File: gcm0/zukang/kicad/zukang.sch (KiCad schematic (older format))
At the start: 109 parts, among them J1 RX, J2 TX, Q1 BC547, Q2 BC547, Q3 BC547, SW1 SW_Push, SW2 SW_Push, U1 74HC595, U10 F5161BS, U11 TL084, U12 TL084, U13 L7805, U14 L7905, U15 LM1117-3.3, U16 STM32F030F4P6, U17 STM32F030F4P6, U2 74HC595, U3 ne602, U4 F5161BS, U5 ne602, U6 CD4052B, U7 F5161BS, U8 F5161BS, U9 F5161BS, Y1 8M, Y2 8M

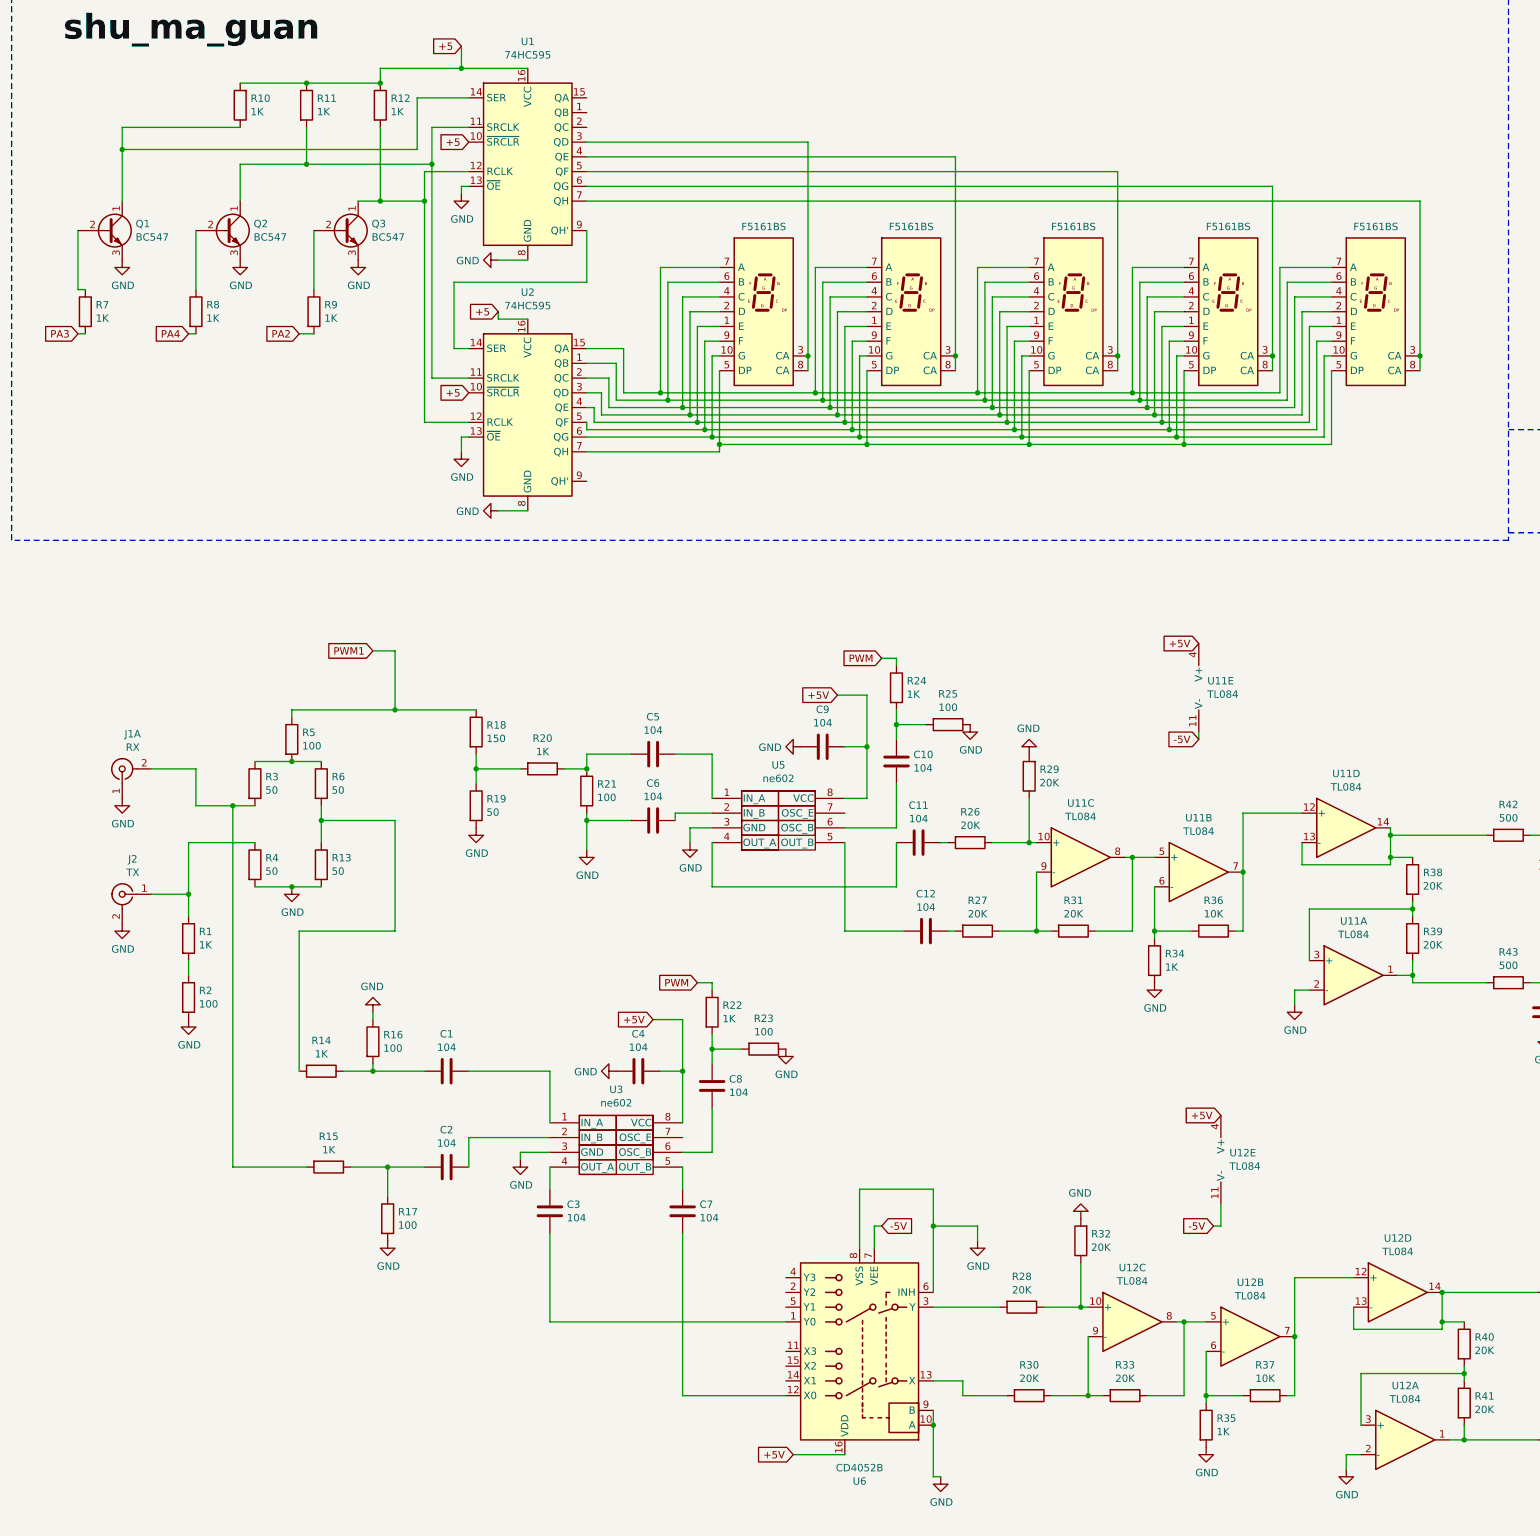
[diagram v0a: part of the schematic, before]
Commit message: 电路改错
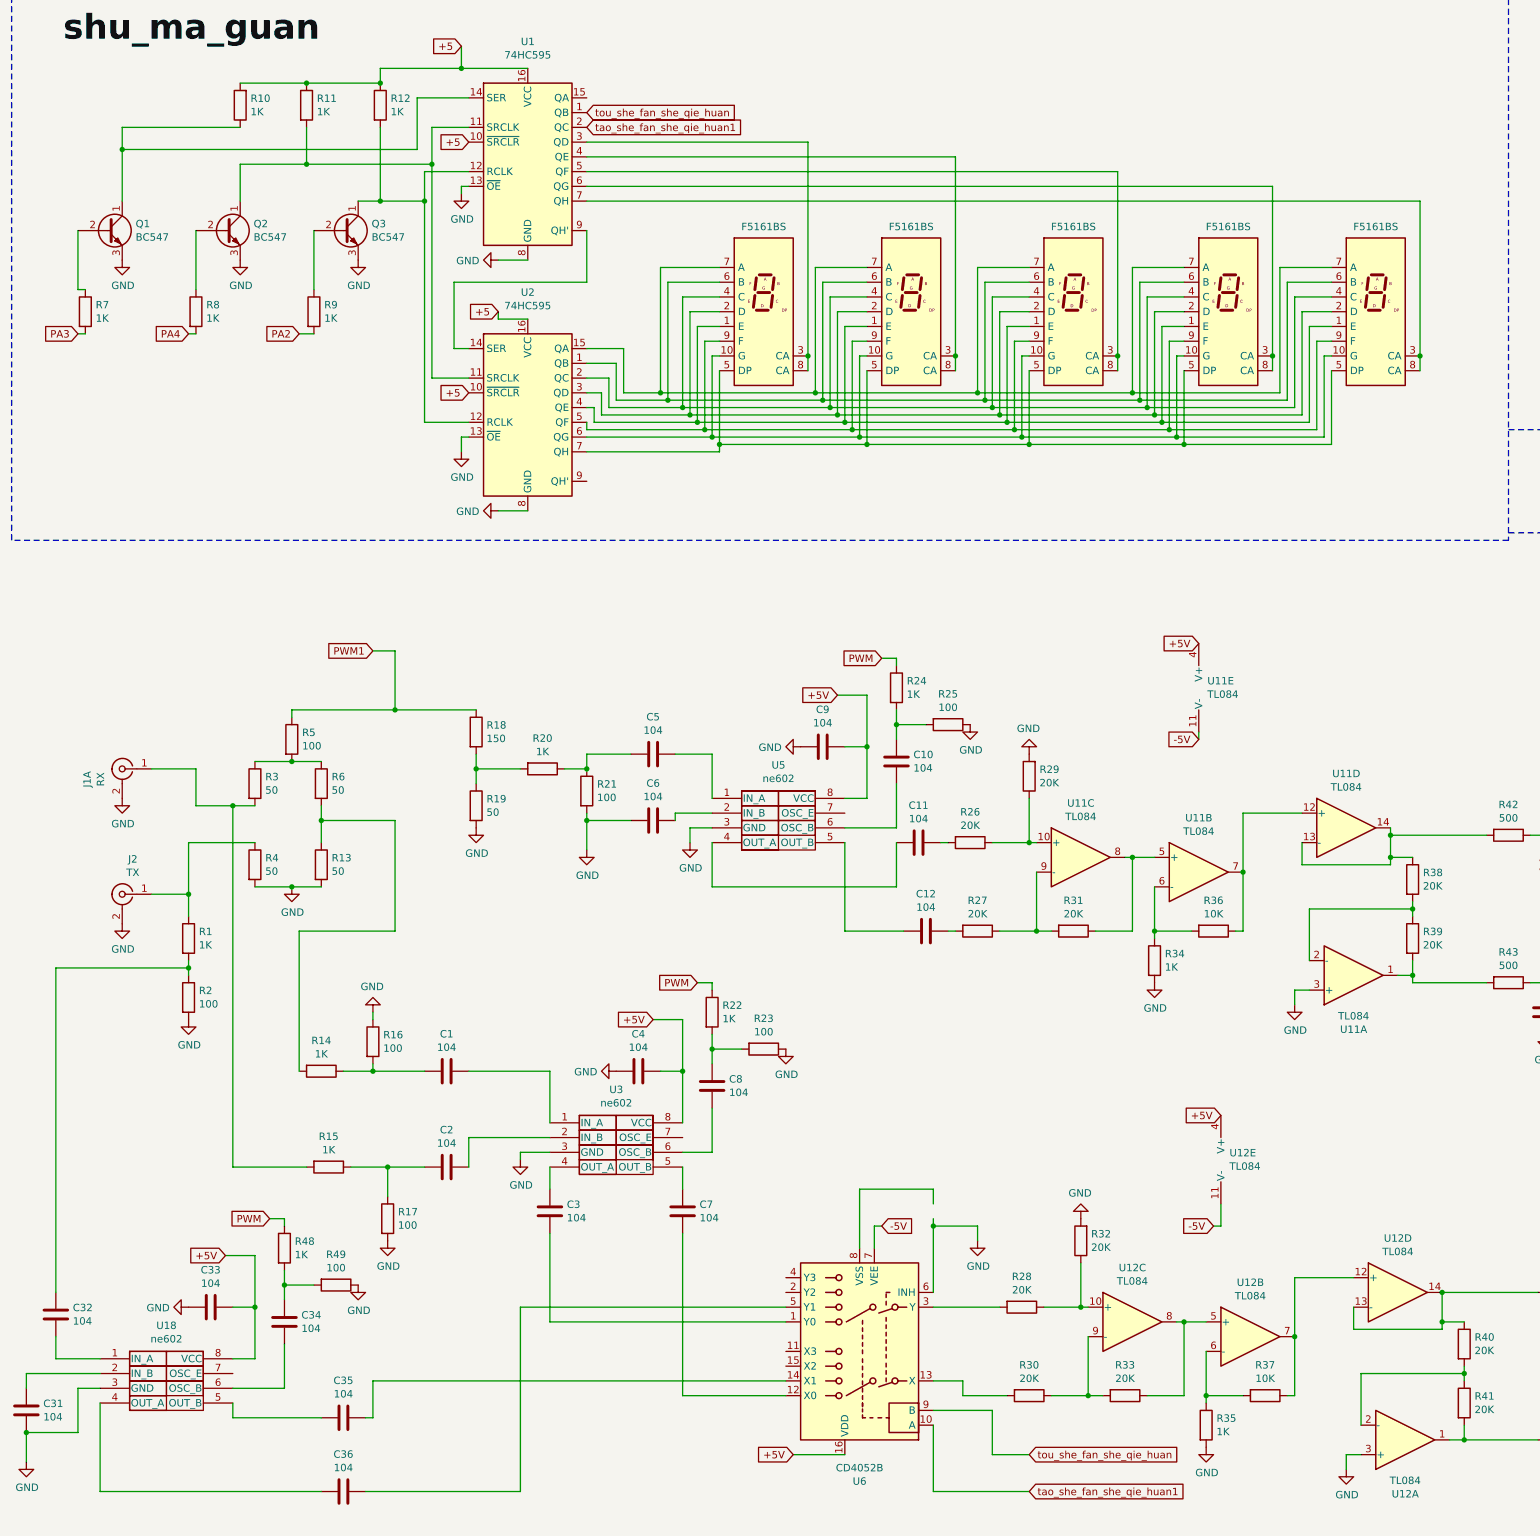
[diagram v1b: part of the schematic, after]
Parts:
- added C31, C32, C33, C34, C35, C36: 104, symbol Device:C
- added R48: 1K, symbol Device:R
- added R49: 100, symbol Device:R
- added U18: ne602, symbol 1-cache:yjmwxwx_ne602
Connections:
- net +5V: now also C33.2, U18.8 (VCC)
- net GND: now also J1.2 (Ext1), U11.3 (+), U12.3 (+), C31.2, C33.1, R49.1, U18.3 (GND); no longer J1.1 (In1), U11.2 (-), U12.2 (-), U6.10 (A), U6.8 (VSS), U6.9 (B)
- net PWM: now also R48.1
- net tou_she_fan_she_qie_huan: now reaches U1.1 (QB)
- net tou_she_fan_she_qie_huan: now also U6.9 (B)
- net tao_she_fan_she_qie_huan1: now reaches U1.2 (QC)
- net tao_she_fan_she_qie_huan1: now also U6.10 (A)
- net at U6.14 (X1): now also C35.1
- net at U6.5 (Y1): now also C36.1
- net at R38.2, R39.1: now also U11.2 (-); no longer U11.3 (+)
- net at R40.2, R41.1: now also U12.2 (-); no longer U12.3 (+)
- net at R15.2, R3.2: now also J1.1 (In1); no longer J1.2 (Ext1)
- net at R1.2, R2.1: now also C32.1
- new net: C32.2, U18.1 (IN_A)
- new net: C31.1, U18.2 (IN_B)
- new net: C36.2, U18.4 (OUT_A)
- new net: C35.2, U18.5 (OUT_B)
- new net: C34.2, U18.6 (OSC_B)
- new net: C34.1, R48.2, R49.2
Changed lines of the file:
@@
 F 3 "http://www.ti.com/lit/ds/symlink/tl081.pdf" H 9700 7450 50  0001 C CNN
 	1    9650 7250
-	1    0    0    -1
+	1    0    0    1
 $EndComp
 $Comp
@@
 F 3 "http://www.ti.com/lit/ds/symlink/tl081.pdf" H 10050 10600 50  0001 C CNN
 	1    10000 10400
-	1    0    0    -1
+	1    0    0    1
 $EndComp
 $Comp
@@
 	6300 8700 6800 8700
 Wire Wire Line
-	6800 8700 6800 8950
+	6800 8700 6800 8800
 $Comp
 L power:GND #PWR0127
@@
 Wire Wire Line
 	6400 8950 6450 8950
-$Comp
-L power:GND #PWR0128
-U 1 1 5FA99091
-P 6850 10650
-F 0 "#PWR0128" H 6850 10400 50  0001 C CNN
-F 1 "GND" H 6855 10477 50  0000 C CNN
-F 2 "" H 6850 10650 50  0001 C CNN
-F 3 "" H 6850 10650 50  0001 C CNN
-	1    6850 10650
-	1    0    0    -1
-$EndComp
-Wire Wire Line
-	6800 10200 6800 10300
-Wire Wire Line
-	6800 10300 6800 10650
-Wire Wire Line
-	6800 10650 6850 10650
-Connection ~ 6800 10300
 Text GLabel 5850 10500 0    50   Input ~ 0
 +5V
@@
 F 3 " ~" H 1300 5850 50  0001 C CNN
 	1    1300 5850
-	0    -1   -1   0
+	-1   0    0    -1
 $EndComp
 $Comp
@@
 $EndComp
 Wire Wire Line
-	1750 7250 1750 7150
+	1750 7250 1750 7200
 Wire Wire Line
 	1750 6850 1750 6700
@@
 Wire Notes Line
 	16000 500  16000 9900
+$Comp
+L 1-cache:yjmwxwx_ne602 U18
+U 1 1 5E485B54
+P 1600 10000
+F 0 "U18" H 1600 10375 50  0000 C CNN
+F 1 "ne602" H 1600 10284 50  0000 C CNN
+F 2 "" H 1550 10300 50  0001 C CNN
+F 3 "" H 1550 10300 50  0001 C CNN
+	1    1600 10000
+	1    0    0    -1
+$EndComp
+$Comp
+L Device:C C36
+U 1 1 5E485B68
+P 2800 10750
+F 0 "C36" V 2548 10750 50  0000 C CNN
+F 1 "104" V 2639 10750 50  0000 C CNN
+F 2 "" H 2838 10600 50  0001 C CNN
+F 3 "~" H 2800 10750 50  0001 C CNN
+	1    2800 10750
+	0    1    1    0
+$EndComp
+$Comp
+L Device:C C35
+U 1 1 5E485B6E
+P 2800 10250
+F 0 "C35" V 2548 10250 50  0000 C CNN
+F 1 "104" V 2639 10250 50  0000 C CNN
+F 2 "" H 2838 10100 50  0001 C CNN
+F 3 "~" H 2800 10250 50  0001 C CNN
+	1    2800 10250
+	0    1    1    0
+$EndComp
+Wire Wire Line
+	2950 10250 3000 10250
+$Comp
+L Device:C C34
+U 1 1 5E485B7B
+P 2400 9600
+F 0 "C34" H 2515 9646 50  0000 L CNN
+F 1 "104" H 2515 9555 50  0000 L CNN
+F 2 "" H 2438 9450 50  0001 C CNN
+F 3 "~" H 2400 9600 50  0001 C CNN
+	1    2400 9600
+	1    0    0    -1
+$EndComp
+Wire Wire Line
+	2400 9750 2400 10050
+Wire Wire Line
+	2400 10050 2050 10050
+$Comp
+L Device:R R48
+U 1 1 5E485B83
+P 2400 9100
+F 0 "R48" H 2470 9146 50  0000 L CNN
+F 1 "1K" H 2470 9055 50  0000 L CNN
+F 2 "" V 2330 9100 50  0001 C CNN
+F 3 "~" H 2400 9100 50  0001 C CNN
+	1    2400 9100
+	1    0    0    -1
+$EndComp
+$Comp
+L Device:R R49
+U 1 1 5E485B89
+P 2750 9350
+F 0 "R49" V 2543 9350 50  0000 C CNN
+F 1 "100" V 2634 9350 50  0000 C CNN
+F 2 "" V 2680 9350 50  0001 C CNN
+F 3 "~" H 2750 9350 50  0001 C CNN
+	1    2750 9350
+	0    1    1    0
+$EndComp
+Wire Wire Line
+	2400 9250 2400 9350
+Wire Wire Line
+	2600 9350 2400 9350
+Connection ~ 2400 9350
+Wire Wire Line
+	2400 9350 2400 9450
+Text GLabel 2300 8900 0    50   Input ~ 0
+PWM
+Wire Wire Line
+	2300 8900 2400 8900
+Wire Wire Line
+	2400 8900 2400 8950
+Text GLabel 2000 9150 0    50   Input ~ 0
++5V
+$Comp
+L Device:C C33
+U 1 1 5E485B97
+P 1900 9500
+F 0 "C33" V 2152 9500 50  0000 C CNN
+F 1 "104" V 2061 9500 50  0000 C CNN
+F 2 "" H 1938 9350 50  0001 C CNN
+F 3 "~" H 1900 9500 50  0001 C CNN
+	1    1900 9500
+	0    -1   -1   0
+$EndComp
+$Comp
+L power:GND #PWR0144
+U 1 1 5E485B9D
+P 1750 9500
+F 0 "#PWR0144" H 1750 9250 50  0001 C CNN
+F 1 "GND" V 1755 9372 50  0000 R CNN
+F 2 "" H 1750 9500 50  0001 C CNN
+F 3 "" H 1750 9500 50  0001 C CNN
+	1    1750 9500
+	0    1    1    0
+$EndComp
+Wire Wire Line
+	2000 9150 2200 9150
+Wire Wire Line
+	2200 9150 2200 9500
+Wire Wire Line
+	2200 9850 2050 9850
+Wire Wire Line
+	2050 9500 2200 9500
+Connection ~ 2200 9500
+Wire Wire Line
+	2200 9500 2200 9850
+$Comp
+L power:GND #PWR0145
+U 1 1 5E485BB9
+P 650 10550
+F 0 "#PWR0145" H 650 10300 50  0001 C CNN
+F 1 "GND" H 655 10377 50  0000 C CNN
+F 2 "" H 650 10550 50  0001 C CNN
+F 3 "" H 650 10550 50  0001 C CNN
+	1    650  10550
+	1    0    0    -1
+$EndComp
+$Comp
+L power:GND #PWR0146
+U 1 1 5E485BDC
+P 2900 9350
+F 0 "#PWR0146" H 2900 9100 50  0001 C CNN
+F 1 "GND" H 2905 9177 50  0000 C CNN
+F 2 "" H 2900 9350 50  0001 C CNN
+F 3 "" H 2900 9350 50  0001 C CNN
+	1    2900 9350
+	1    0    0    -1
+$EndComp
+Wire Wire Line
+	1000 10050 1150 10050
+$Comp
+L Device:C C32
+U 1 1 5E7B8D18
+P 850 9550
+F 0 "C32" H 965 9596 50  0000 L CNN
+F 1 "104" H 965 9505 50  0000 L CNN
+F 2 "" H 888 9400 50  0001 C CNN
+F 3 "~" H 850 9550 50  0001 C CNN
+	1    850  9550
+	1    0    0    -1
+$EndComp
+$Comp
+L Device:C C31
+U 1 1 5E7BB19E
+P 650 10200
+F 0 "C31" H 765 10246 50  0000 L CNN
+F 1 "104" H 765 10155 50  0000 L CNN
+F 2 "" H 688 10050 50  0001 C CNN
+F 3 "~" H 650 10200 50  0001 C CNN
+	1    650  10200
+	1    0    0    -1
+$EndComp
+Wire Wire Line
+	1000 10350 650  10350
+Wire Wire Line
+	650  10550 650  10350
+Connection ~ 650  10350
+Wire Wire Line
+	650  10050 650  9950
+Wire Wire Line
+	650  9950 1150 9950
+Wire Wire Line
+	1000 10050 1000 10350
+Wire Wire Line
+	1150 9850 850  9850
+Wire Wire Line
+	850  9850 850  9700
+Wire Wire Line
+	850  9400 850  7200
+Wire Wire Line
+	850  7200 1750 7200
+Connection ~ 1750 7200
+Wire Wire Line
+	1750 7200 1750 7150
+Wire Wire Line
+	2050 10150 2050 10250
+Wire Wire Line
+	2050 10250 2650 10250
+Wire Wire Line
+	1150 10750 2650 10750
+Wire Wire Line
+	1150 10150 1150 10750
+Wire Wire Line
+	2950 10750 4000 10750
+Wire Wire Line
+	4000 10750 4000 9500
+Wire Wire Line
+	4000 9500 5800 9500
+Wire Wire Line
+	3000 10250 3000 10000
+Wire Wire Line
+	3000 10000 5800 10000
+Wire Wire Line
+	6800 8900 6800 8950
+Text GLabel 7450 10500 2    50   Input ~ 0
+tou_she_fan_she_qie_huan
+Text GLabel 7450 10750 2    50   Input ~ 0
+tao_she_fan_she_qie_huan1
+Wire Wire Line
+	7450 10500 7200 10500
+Wire Wire Line
+	7200 10500 7200 10200
+Wire Wire Line
+	7200 10200 6800 10200
+Wire Wire Line
+	7450 10750 6800 10750
+Wire Wire Line
+	6800 10750 6800 10300
+Text GLabel 4450 1400 2    50   Input ~ 0
+tou_she_fan_she_qie_huan
+Text GLabel 4450 1500 2    50   Input ~ 0
+tao_she_fan_she_qie_huan1
 $EndSCHEMATC

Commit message: 加入透射
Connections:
- net GND: now also U6.9 (B)
- net tou_she_fan_she_qie_huan: now also U1.15 (QA), U6.10 (A); no longer U1.1 (QB), U6.9 (B)
- net tao_she_fan_she_qie_huan1: no longer names the net of U1.2 (QC)
- net tao_she_fan_she_qie_huan1: no longer U6.10 (A)
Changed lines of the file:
@@
 Wire Wire Line
 	6800 8900 6800 8950
-Text GLabel 7450 10500 2    50   Input ~ 0
+Text GLabel 7450 10750 2    50   Input ~ 0
 tou_she_fan_she_qie_huan
-Text GLabel 7450 10750 2    50   Input ~ 0
-tao_she_fan_she_qie_huan1
-Wire Wire Line
-	7450 10500 7200 10500
-Wire Wire Line
-	7200 10500 7200 10200
 Wire Wire Line
 	7200 10200 6800 10200
@@
 Wire Wire Line
 	6800 10750 6800 10300
-Text GLabel 4450 1400 2    50   Input ~ 0
+Text GLabel 4450 1300 2    50   Input ~ 0
 tou_she_fan_she_qie_huan
-Text GLabel 4450 1500 2    50   Input ~ 0
-tao_she_fan_she_qie_huan1
+$Comp
+L power:GND #PWR?
+U 1 1 5E67A733
+P 7200 10200
+F 0 "#PWR?" H 7200 9950 50  0001 C CNN
+F 1 "GND" H 7205 10027 50  0000 C CNN
+F 2 "" H 7200 10200 50  0001 C CNN
+F 3 "" H 7200 10200 50  0001 C CNN
+	1    7200 10200
+	1    0    0    -1
+$EndComp
 $EndSCHEMATC
